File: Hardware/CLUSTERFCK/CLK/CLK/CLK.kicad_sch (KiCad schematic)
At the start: 46 parts

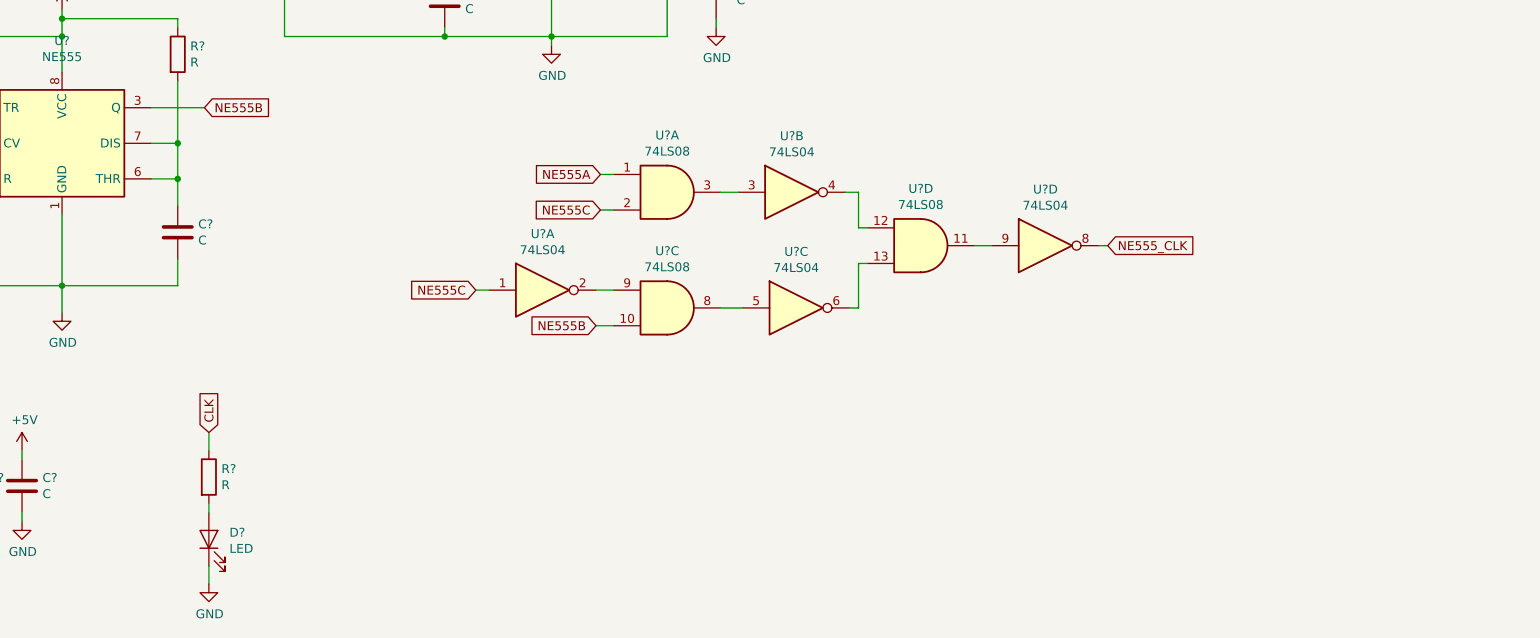
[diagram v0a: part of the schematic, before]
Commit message: 16 | 1h | Added powerSupply to CLK module
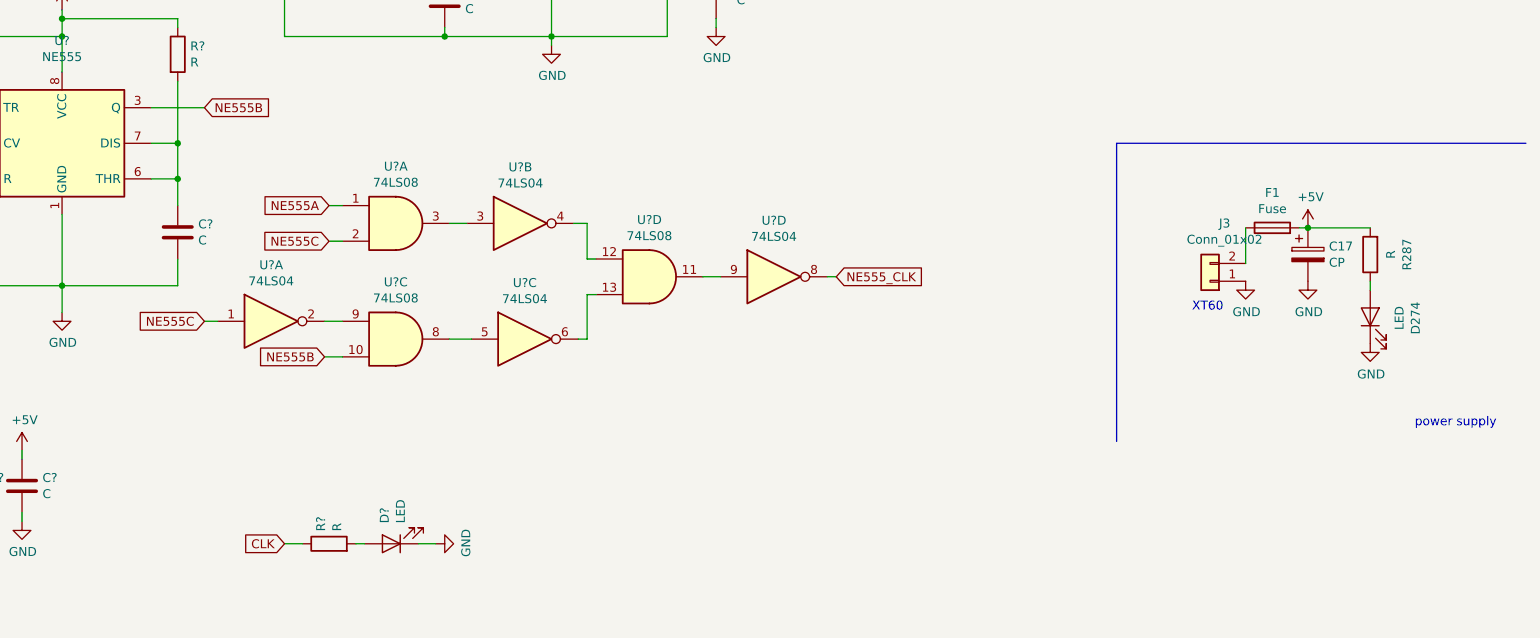
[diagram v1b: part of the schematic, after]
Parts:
- added C17: CP, Capacitor_Tantalum_SMD:CP_EIA-6032-15_Kemet-U_Pad2.25x2.35mm_HandSolder, symbol Device:CP
- added D274: LED, LED_THT:LED_D5.0mm, symbol Device:LED
- added F1: Fuse, Fuse:Fuse_1812_4532Metric_Pad1.30x3.40mm_HandSolder, symbol Device:Fuse
- added J3: Conn_01x02, Connector_AMASS:AMASS_XT30U-F_1x02_P5.0mm_Vertical, symbol Connector_Generic:Conn_01x02
- added R287: R, Resistor_SMD:R_0805_2012Metric_Pad1.15x1.40mm_HandSolder, symbol Device:R
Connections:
- net +5V: now also C17.1, F1.2, R287.2
- net GND: now also C17.2, D274.1 (K), J3.1 (Pin_1)
- new net: D274.2 (A), R287.1
- new net: F1.1, J3.2 (Pin_2)
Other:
- note added: "XT60"
- note added: "power supply"
- moved on the sheet: D?, R?, U?A, U?B, U?C, U?D
